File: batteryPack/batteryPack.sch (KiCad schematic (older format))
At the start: 2 parts

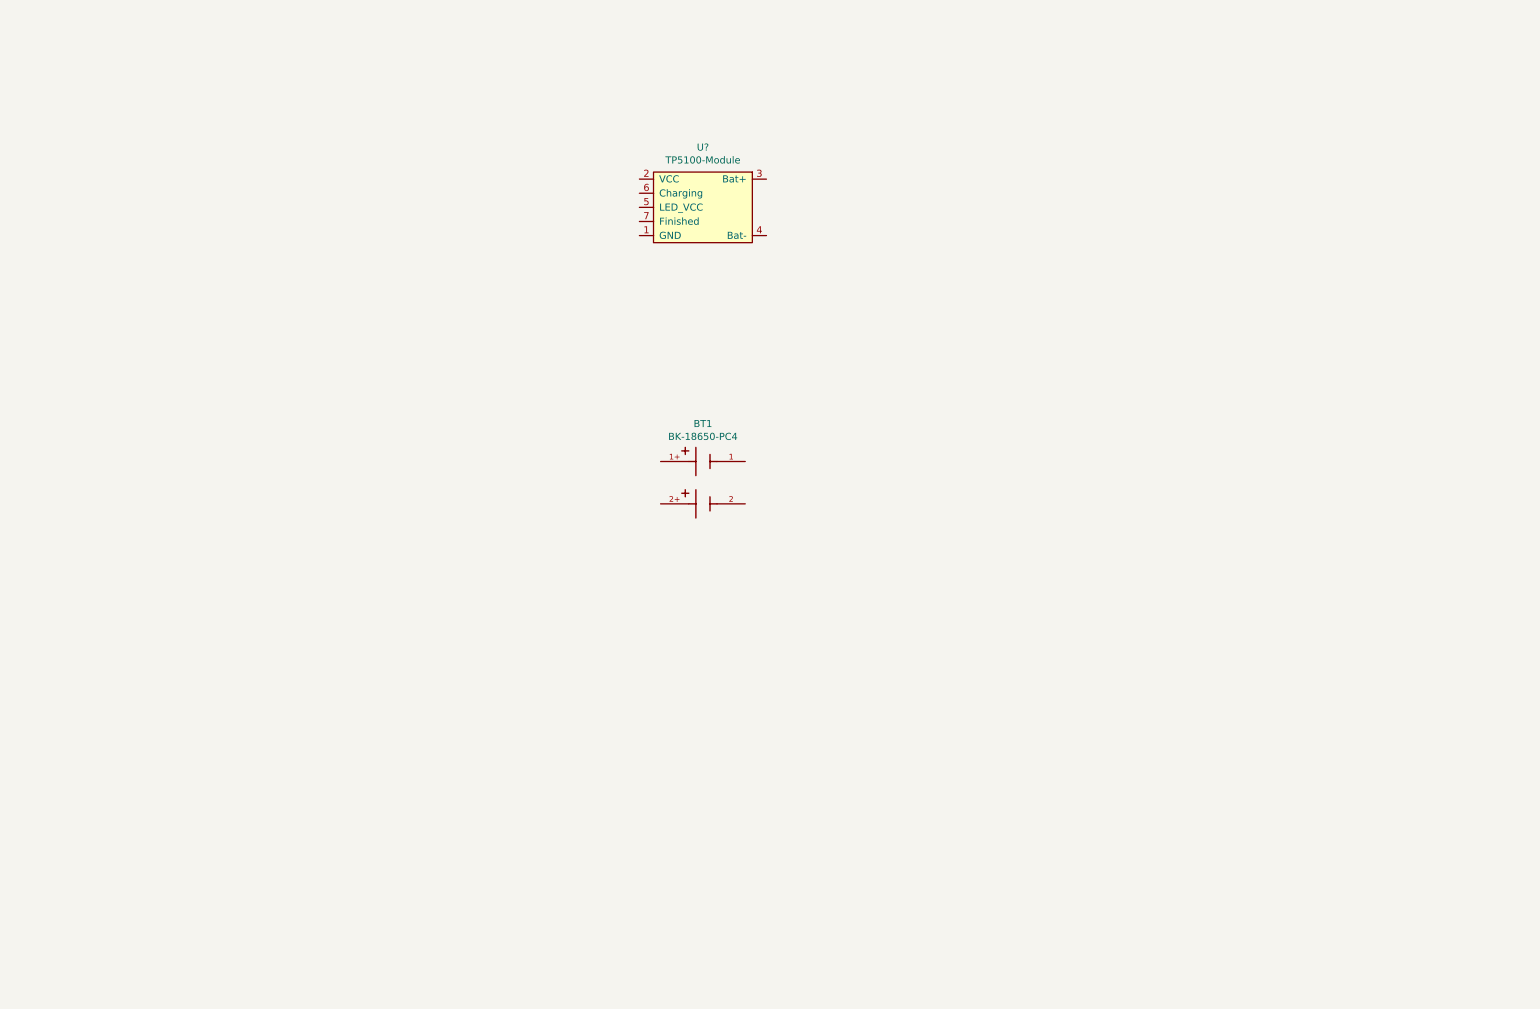
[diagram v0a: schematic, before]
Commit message: Finish first draft of the schematics
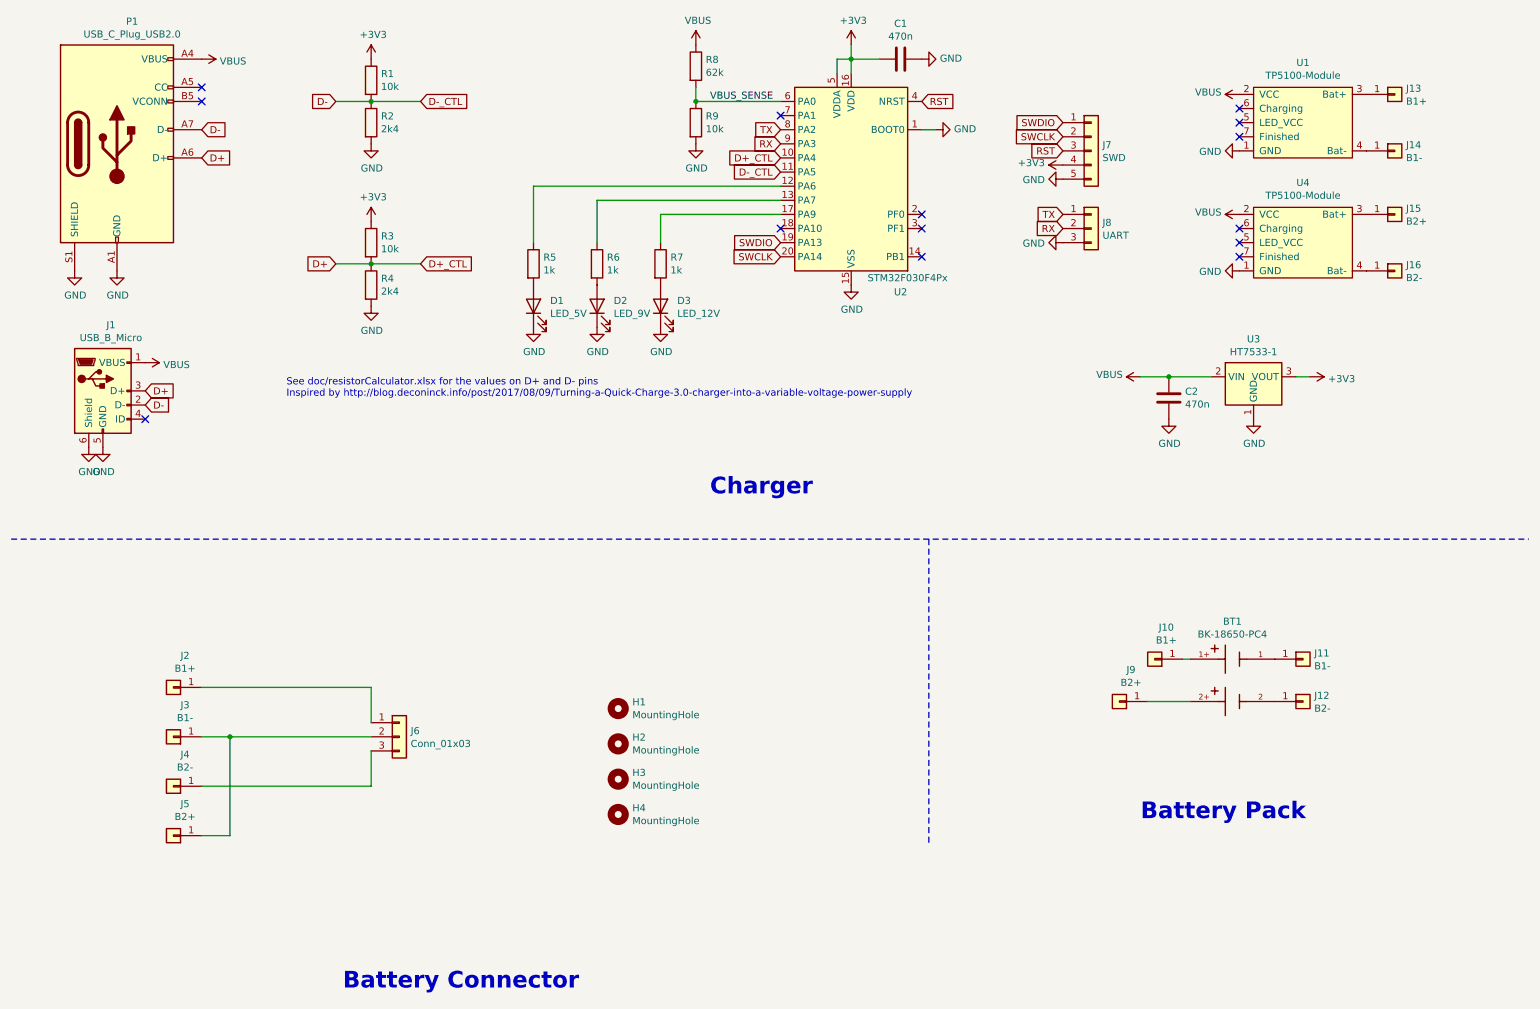
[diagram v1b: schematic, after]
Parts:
- added C1, C2: 470n, Capacitor_SMD:C_0603_1608Metric_Pad1.05x0.95mm_HandSolder, symbol Device:C
- added D1: LED_5V, LED_SMD:LED_0603_1608Metric_Pad1.05x0.95mm_HandSolder, symbol Device:LED
- added D2: LED_9V, LED_SMD:LED_0603_1608Metric_Pad1.05x0.95mm_HandSolder, symbol Device:LED
- added D3: LED_12V, LED_SMD:LED_0603_1608Metric_Pad1.05x0.95mm_HandSolder, symbol Device:LED
- added H1, H2, H3, H4: MountingHole, MountingHole:MountingHole_3.2mm_M3, symbol Mechanical:MountingHole
- added J1: USB_B_Micro, Connector_USB:USB_Micro-B_Wuerth_629105150521_CircularHoles, symbol Connector:USB_B_Micro
- added J10: B1+, batteryPack:2mm_Banana-Socket, symbol Connector_Generic:Conn_01x01
- added J11: B1-, batteryPack:2mm_Banana-Socket, symbol Connector_Generic:Conn_01x01
- added J12: B2-, batteryPack:2mm_Banana-Socket, symbol Connector_Generic:Conn_01x01
- added J13: B1+, batteryPack:2mm_Banana-Plug, symbol Connector_Generic:Conn_01x01
- added J14: B1-, batteryPack:2mm_Banana-Plug, symbol Connector_Generic:Conn_01x01
- added J15: B2+, batteryPack:2mm_Banana-Plug, symbol Connector_Generic:Conn_01x01
- added J16: B2-, batteryPack:2mm_Banana-Plug, symbol Connector_Generic:Conn_01x01
- added J2: B1+, batteryPack:2mm_Banana-Vertical, symbol Connector_Generic:Conn_01x01
- added J3: B1-, batteryPack:2mm_Banana-Vertical, symbol Connector_Generic:Conn_01x01
- added J4: B2-, batteryPack:2mm_Banana-Vertical, symbol Connector_Generic:Conn_01x01
- added J5: B2+, batteryPack:2mm_Banana-Vertical, symbol Connector_Generic:Conn_01x01
- added J6: Conn_01x03, batteryPack:cableConnector, symbol Connector_Generic:Conn_01x03
- added J7: SWD, Connector_PinHeader_2.54mm:PinHeader_1x05_P2.54mm_Vertical, symbol Connector_Generic:Conn_01x05
- added J8: UART, Connector_PinHeader_2.54mm:PinHeader_1x03_P2.54mm_Vertical, symbol Connector_Generic:Conn_01x03
- added J9: B2+, batteryPack:2mm_Banana-Socket, symbol Connector_Generic:Conn_01x01
- added P1: USB_C_Plug_USB2.0, batteryPack:USB_C_Female-16Pin-HPJF, symbol Connector:USB_C_Plug_USB2.0
- added R1, R3, R9: 10k, Resistor_SMD:R_0603_1608Metric_Pad1.05x0.95mm_HandSolder, symbol Device:R
- added R2, R4: 2k4, Resistor_SMD:R_0603_1608Metric_Pad1.05x0.95mm_HandSolder, symbol Device:R
- added R5, R6, R7: 1k, Resistor_SMD:R_0603_1608Metric_Pad1.05x0.95mm_HandSolder, symbol Device:R
- added R8: 62k, Resistor_SMD:R_0603_1608Metric_Pad1.05x0.95mm_HandSolder, symbol Device:R
- added U2: STM32F030F4Px, Package_SO:TSSOP-20_4.4x6.5mm_P0.65mm, symbol MCU_ST_STM32F0:STM32F030F4Px
- added U3: HT7533-1, Package_TO_SOT_SMD:SOT-89-3, symbol Regulator_Linear:HT75xx-1-SOT89
- added U4: TP5100-Module, batteryPack:TP5100-Module, symbol batteryPack:TP5100-Module
- gave numbers to parts that had none: 1
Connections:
- net at BT1.1 (1-): now also J11.1 (Pin_1)
- net at BT1.1+: now also J10.1 (Pin_1)
- net at BT1.2 (2-): now also J12.1 (Pin_1)
- net at BT1.2+: now also J9.1 (Pin_1)
- net GND: now reaches U1.1 (GND)
- net GND: now also C1.1, C2.1, D1.1 (K), D2.1 (K), D3.1 (K), J1.5 (GND), J1.6 (Shield), J7.5 (Pin_5), J8.3 (Pin_3), P1.A1 (GND), P1.A12 (GND), P1.B1 (GND), P1.B12 (GND), P1.S1 (SHIELD), R2.2, R4.2, R9.2, U2.1 (BOOT0), U2.15 (VSS), U3.1 (GND), U4.1 (GND)
- net VBUS: now reaches U1.2 (VCC)
- net VBUS: now also C2.2, J1.1 (VBUS), P1.A4 (VBUS), P1.A9 (VBUS), P1.B4 (VBUS), P1.B9 (VBUS), R8.1, U3.2 (VIN), U4.2 (VCC)
- net at U1.3 (Bat+): now also J13.1 (Pin_1)
- net at U1.4 (Bat-): now also J14.1 (Pin_1)
- new net: J15.1 (Pin_1), U4.3 (Bat+)
- new net: J16.1 (Pin_1), U4.4 (Bat-)
- new net: R5.1, U2.12 (PA6)
- new net: R6.1, U2.13 (PA7)
- new net: R7.1, U2.17 (PA9)
- new net: D1.2 (A), R5.2
- new net: D2.2 (A), R6.2
- new net: D3.2 (A), R7.2
- new net: J3.1 (Pin_1), J5.1 (Pin_1), J6.2 (Pin_2)
- new net: J2.1 (Pin_1), J6.1 (Pin_1)
- new net: J4.1 (Pin_1), J6.3 (Pin_3)
- new net +3V3: C1.2, J7.4 (Pin_4), R1.1, R3.1, U2.16 (VDD), U2.5 (VDDA), U3.3 (VOUT)
- new net D+: J1.3 (D+), P1.A6 (D+), R3.2, R4.1, U2.10 (PA4)
- new net D-: J1.2 (D-), P1.A7 (D-), R1.2, R2.1, U2.11 (PA5)
- new net RST: J7.3 (Pin_3), U2.4 (NRST)
- new net RX: J8.2 (Pin_2), U2.9 (PA3)
- new net SWCLK: J7.2 (Pin_2), U2.20 (PA14)
- new net SWDIO: J7.1 (Pin_1), U2.19 (PA13)
- new net TX: J8.1 (Pin_1), U2.8 (PA2)
- new net VBUS_SENSE: R8.2, R9.1, U2.6 (PA0)
- no-connect marks 0 -> 14
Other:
- note added: "Battery Connector"
- note added: "Battery Pack"
- note added: "Charger"
- note added: "See doc/resistorCalculator.xlsx for the values on D+ and D- pins\nInspired by http://blog.deconinck.info/post/2017/08/09/Turning-a-Quick-Charge-3.0-charger-into-a-variable-voltage-power-supply"
- moved on the sheet: BT1, U1

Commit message: Sketch out initial component layout
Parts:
- J6: value Conn_01x03 -> CableConnector
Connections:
- net MID: now reaches J3.1 (Pin_1), J5.1 (Pin_1), J6.2 (Pin_2)
- net OUT+: now reaches J2.1 (Pin_1), J6.1 (Pin_1)
- net OUT-: now reaches J4.1 (Pin_1), J6.3 (Pin_3)
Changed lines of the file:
@@
 P 3250 5750
 F 0 "J6" H 3330 5792 50  0000 L CNN
-F 1 "Conn_01x03" H 3330 5701 50  0000 L CNN
+F 1 "CableConnector" H 3330 5701 50  0000 L CNN
 F 2 "batteryPack:cableConnector" H 3250 5750 50  0001 C CNN
 F 3 "~" H 3250 5750 50  0001 C CNN
@@
 	0    -1   -1   0
 $EndComp
+Text Label 2850 5400 0    50   ~ 0
+OUT+
+Text Label 2850 6100 0    50   ~ 0
+OUT-
+Text Label 2850 5750 0    50   ~ 0
+MID
 $EndSCHEMATC

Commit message: Route battery and the connector
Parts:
- removed H3, H4: MountingHole, MountingHole:MountingHole_3.2mm_M3, symbol Mechanical:MountingHole
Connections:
- net BP_B1-: now reaches BT1.1 (1-), J11.1 (Pin_1)
- net BP_B1+: now reaches BT1.1+, J10.1 (Pin_1)
- net BP_B2-: now reaches BT1.2 (2-), J12.1 (Pin_1)
- net BP_B2+: now reaches BT1.2+, J9.1 (Pin_1)
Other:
- moved on the sheet: J10, J11, J12
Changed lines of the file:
@@
 L Connector_Generic:Conn_01x01 J10
 U 1 1 5E83A998
-P 8600 5200
-F 0 "J10" H 8518 4975 50  0000 C CNN
-F 1 "B1+" H 8518 5066 50  0000 C CNN
-F 2 "batteryPack:2mm_Banana-Socket" H 8600 5200 50  0001 C CNN
-F 3 "~" H 8600 5200 50  0001 C CNN
-	1    8600 5200
+P 8200 5200
+F 0 "J10" H 8118 4975 50  0000 C CNN
+F 1 "B1+" H 8118 5066 50  0000 C CNN
+F 2 "batteryPack:2mm_Banana-Socket" H 8200 5200 50  0001 C CNN
+F 3 "~" H 8200 5200 50  0001 C CNN
+	1    8200 5200
 	-1   0    0    1
 $EndComp
@@
 L Connector_Generic:Conn_01x01 J11
 U 1 1 5E83B363
-P 9650 5200
-F 0 "J11" H 9730 5242 50  0000 L CNN
-F 1 "B1-" H 9730 5151 50  0000 L CNN
-F 2 "batteryPack:2mm_Banana-Socket" H 9650 5200 50  0001 C CNN
-F 3 "~" H 9650 5200 50  0001 C CNN
-	1    9650 5200
+P 10400 5200
+F 0 "J11" H 10480 5242 50  0000 L CNN
+F 1 "B1-" H 10480 5151 50  0000 L CNN
+F 2 "batteryPack:2mm_Banana-Socket" H 10400 5200 50  0001 C CNN
+F 3 "~" H 10400 5200 50  0001 C CNN
+	1    10400 5200
 	1    0    0    -1
 $EndComp
@@
 L Connector_Generic:Conn_01x01 J12
 U 1 1 5E83B842
-P 9650 5500
-F 0 "J12" H 9730 5542 50  0000 L CNN
-F 1 "B2-" H 9730 5451 50  0000 L CNN
-F 2 "batteryPack:2mm_Banana-Socket" H 9650 5500 50  0001 C CNN
-F 3 "~" H 9650 5500 50  0001 C CNN
-	1    9650 5500
-	1    0    0    -1
-$EndComp
-Wire Wire Line
-	8850 5200 8800 5200
+P 10200 5500
+F 0 "J12" H 10280 5542 50  0000 L CNN
+F 1 "B2-" H 10280 5451 50  0000 L CNN
+F 2 "batteryPack:2mm_Banana-Socket" H 10200 5500 50  0001 C CNN
+F 3 "~" H 10200 5500 50  0001 C CNN
+	1    10200 5500
+	1    0    0    -1
+$EndComp
+Wire Wire Line
+	8850 5200 8400 5200
 Wire Wire Line
 	8850 5500 8550 5500
@@
 	1    0    0    -1
 $EndComp
-$Comp
-L Mechanical:MountingHole H3
-U 1 1 5EA16A2A
-P 4800 6050
-F 0 "H3" H 4900 6096 50  0000 L CNN
-F 1 "MountingHole" H 4900 6005 50  0000 L CNN
-F 2 "MountingHole:MountingHole_3.2mm_M3" H 4800 6050 50  0001 C CNN
-F 3 "~" H 4800 6050 50  0001 C CNN
-	1    4800 6050
-	1    0    0    -1
-$EndComp
-$Comp
-L Mechanical:MountingHole H4
-U 1 1 5EA17F6A
-P 4800 6300
-F 0 "H4" H 4900 6346 50  0000 L CNN
-F 1 "MountingHole" H 4900 6255 50  0000 L CNN
-F 2 "MountingHole:MountingHole_3.2mm_M3" H 4800 6300 50  0001 C CNN
-F 3 "~" H 4800 6300 50  0001 C CNN
-	1    4800 6300
-	1    0    0    -1
-$EndComp
 Wire Wire Line
 	1850 5750 2050 5750
@@
 Text Label 2850 5750 0    50   ~ 0
 MID
+Wire Wire Line
+	10200 5200 9450 5200
+Wire Wire Line
+	10000 5500 9450 5500
+Text Label 8550 5500 0    50   ~ 0
+BP_B2+
+Text Label 9600 5500 0    50   ~ 0
+BP_B2-
+Text Label 9600 5200 0    50   ~ 0
+BP_B1-
+Text Label 8550 5200 0    50   ~ 0
+BP_B1+
 $EndSCHEMATC

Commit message: Route the charger
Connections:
- net SWCLK: now also J7.1 (Pin_1); no longer J7.2 (Pin_2)
- net SWDIO: now also J7.2 (Pin_2); no longer J7.1 (Pin_1)
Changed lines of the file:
@@
 	0    1    1    0
 $EndComp
-Text GLabel 1850 1450 2    50   Input ~ 0
+Text GLabel 2000 1450 2    50   Input ~ 0
 D-
-Text GLabel 1850 1650 2    50   Input ~ 0
+Text GLabel 2000 1650 2    50   Input ~ 0
 D+
 Text GLabel 1450 3400 2    50   Input ~ 0
@@
 Text GLabel 5950 2250 0    50   Input ~ 0
 SWDIO
+Text GLabel 7950 1500 0    50   Input ~ 0
+SWDIO
 Text GLabel 7950 1400 0    50   Input ~ 0
-SWDIO
-Text GLabel 7950 1500 0    50   Input ~ 0
 SWCLK
 $Comp
@@
 Text Label 8550 5200 0    50   ~ 0
 BP_B1+
+Wire Wire Line
+	2000 1450 1850 1450
+Wire Wire Line
+	2000 1650 1850 1650
 $EndSCHEMATC

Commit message: Fine tune the board based on the feedback
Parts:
- J1: value USB_B_Micro -> Mirco USB
- P1: value USB_C_Plug_USB2.0 -> USB-C; symbol Connector:USB_C_Plug_USB2.0 -> Connector:USB_C_Receptacle_USB2.0
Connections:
- net D+: now also P1.B6 (D+)
- net D-: now also P1.B7 (D-)
- net B1_CH: now reaches U1.6 (Charging)
- net B1_CH: now also U2.2 (PF0)
- net B1_F: now reaches U1.7 (Finished)
- net B1_F: now also U2.3 (PF1)
- net B2_CH: now reaches U4.6 (Charging)
- net B2_CH: now also U2.18 (PA10)
- net B2_F: now reaches U4.7 (Finished)
- net B2_F: now also U2.14 (PB1)
- no-connect marks 14 -> 8
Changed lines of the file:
@@
 	1    0    0    -1
 $EndComp
-NoConn ~ 9200 1300
 NoConn ~ 9200 1400
-NoConn ~ 9200 1500
-NoConn ~ 9200 2150
 NoConn ~ 9200 2250
-NoConn ~ 9200 2350
-$Comp
-L Connector:USB_C_Plug_USB2.0 P1
+$Comp
+L Connector:USB_C_Receptacle_USB2.0 P1
 U 1 1 5E8413A8
 P 1250 1550
 F 0 "P1" H 1357 2417 50  0000 C CNN
-F 1 "USB_C_Plug_USB2.0" H 1357 2326 50  0000 C CNN
+F 1 "USB-C" H 1357 2326 50  0000 C CNN
 F 2 "batteryPack:USB_C_Female-16Pin-HPJF" H 1400 1550 50  0001 C CNN
 F 3 "https://www.usb.org/sites/default/files/documents/usb_type-c.zip" H 1400 1550 50  0001 C CNN
@@
 P 1150 3300
 F 0 "J1" H 1207 3767 50  0000 C CNN
-F 1 "USB_B_Micro" H 1207 3676 50  0000 C CNN
+F 1 "Mirco USB" H 1207 3676 50  0000 C CNN
 F 2 "Connector_USB:USB_Micro-B_Wuerth_629105150521_CircularHoles" H 1300 3250 50  0001 C CNN
 F 3 "~" H 1300 3250 50  0001 C CNN
@@
 D-_CTL
 NoConn ~ 5950 1350
-NoConn ~ 5950 2150
-NoConn ~ 6950 2350
-NoConn ~ 6950 2150
-NoConn ~ 6950 2050
 $Comp
 L Device:LED D1
@@
 Wire Wire Line
 	2000 1650 1850 1650
+NoConn ~ 1850 2050
+NoConn ~ 1850 2150
+Wire Wire Line
+	1850 1550 1850 1450
+Connection ~ 1850 1450
+Wire Wire Line
+	1850 1750 1850 1650
+Connection ~ 1850 1650
+Text GLabel 6950 2050 2    50   Input ~ 0
+B1_CH
+Text GLabel 9200 1500 0    50   Input ~ 0
+B1_F
+Text GLabel 9200 2150 0    50   Input ~ 0
+B2_CH
+Text GLabel 9200 2350 0    50   Input ~ 0
+B2_F
+Text GLabel 9200 1300 0    50   Input ~ 0
+B1_CH
+Text GLabel 6950 2150 2    50   Input ~ 0
+B1_F
+Text GLabel 5950 2150 0    50   Input ~ 0
+B2_CH
+Text GLabel 6950 2350 2    50   Input ~ 0
+B2_F
 $EndSCHEMATC

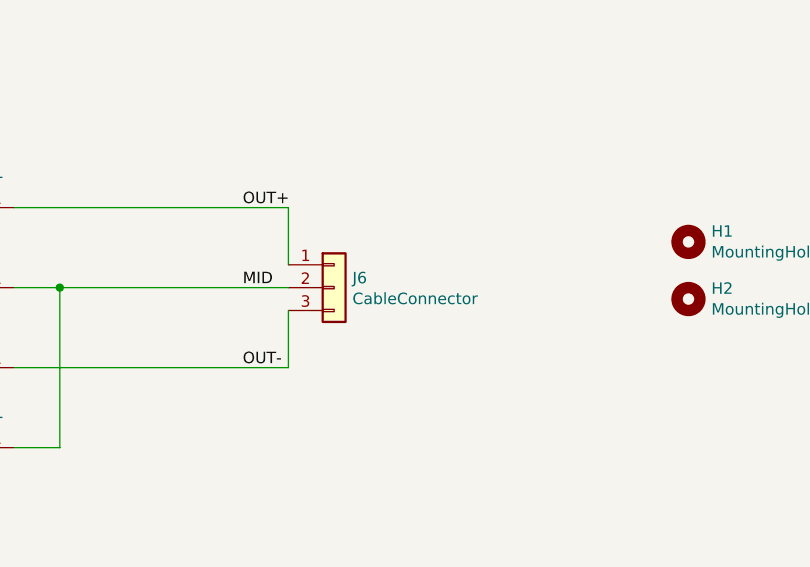
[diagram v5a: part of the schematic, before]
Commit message: Change connector to screw terminal
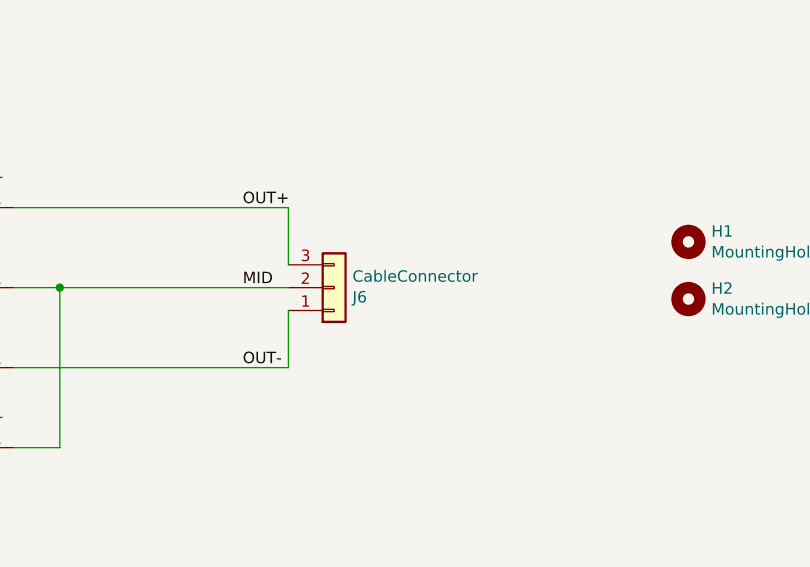
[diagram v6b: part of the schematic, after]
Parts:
- J6: footprint batteryPack:cableConnector -> batteryPack:Terminal_1x03_P5.08mm_Horizontal
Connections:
- net OUT+: now also J6.3 (Pin_3); no longer J6.1 (Pin_1)
- net OUT-: now also J6.1 (Pin_1); no longer J6.3 (Pin_3)
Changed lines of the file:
@@
 Wire Wire Line
 	2050 6450 1850 6450
-$Comp
-L Connector_Generic:Conn_01x03 J6
-U 1 1 5EA258DB
-P 3250 5750
-F 0 "J6" H 3330 5792 50  0000 L CNN
-F 1 "CableConnector" H 3330 5701 50  0000 L CNN
-F 2 "batteryPack:cableConnector" H 3250 5750 50  0001 C CNN
-F 3 "~" H 3250 5750 50  0001 C CNN
-	1    3250 5750
-	1    0    0    -1
-$EndComp
 Wire Wire Line
 	3050 5750 2050 5750
@@
 Text GLabel 6950 2350 2    50   Input ~ 0
 B2_F
+$Comp
+L Connector_Generic:Conn_01x03 J6
+U 1 1 5EA258DB
+P 3250 5750
+F 0 "J6" H 3330 5792 50  0000 L CNN
+F 1 "CableConnector" H 3330 5701 50  0000 L CNN
+F 2 "batteryPack:Terminal_1x03_P5.08mm_Horizontal" H 3250 5750 50  0001 C CNN
+F 3 "~" H 3250 5750 50  0001 C CNN
+	1    3250 5750
+	1    0    0    1
+$EndComp
 $EndSCHEMATC
